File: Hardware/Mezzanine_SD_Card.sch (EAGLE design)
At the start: 9 parts, among them U1 USD-SOCKETNEW, U2 EDISON_CONNECTOR_FULLMOUNTING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, U3 EDISON_CONNECTOR_FULLHEADER

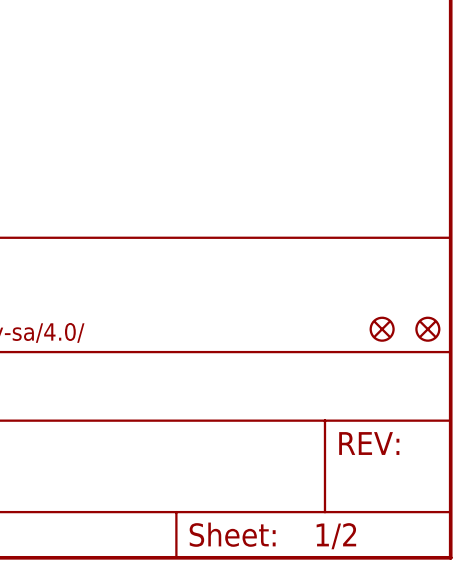
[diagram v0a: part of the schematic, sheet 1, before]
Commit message: added fiducials
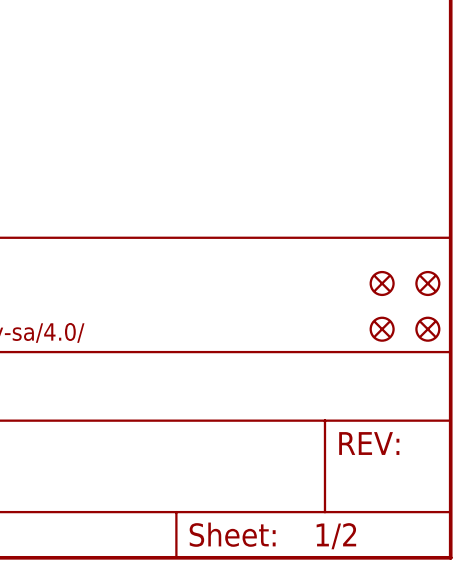
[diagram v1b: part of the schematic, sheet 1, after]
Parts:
- added FID3, FID4: FIDUCIAL1X2, SparkFun-Aesthetics:FIDUCIAL1X2
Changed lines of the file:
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@@
 <part name="U1" library="SparkFun-Connectors" deviceset="USD-SOCKET" device="NEW"/>
 <part name="GND1" library="SparkFun-Aesthetics" deviceset="GND" device=""/>
+<part name="FID3" library="SparkFun-Aesthetics" deviceset="FIDUCIAL" device="1X2"/>
+<part name="FID4" library="SparkFun-Aesthetics" deviceset="FIDUCIAL" device="1X2"/>
 </parts>
 <sheets>
@@
 <instance part="U1" gate="G$1" x="160.02" y="111.76"/>
 <instance part="GND1" gate="1" x="147.32" y="88.9"/>
+<instance part="FID3" gate="G$1" x="246.38" y="30.48"/>
+<instance part="FID4" gate="G$1" x="241.3" y="30.48"/>
 </instances>
 <busses>

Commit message: Layout complete, Ready for review.
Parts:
- added C1, C2: 0.1uF, SparkFun-Capacitors:0.1UF-25V(+80/-20%)(0603)
- added U$1: TXB0108, Testing:TXB0108
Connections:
- new net N$1: U$1.B1, U1.NC
- new net N$2: U$1.B2, U1.CS
- new net N$3: U$1.B3, U1.DI
- new net N$4: U$1.B4, U1.SCK
- new net N$5: U$1.B5, U1.DO
- new net N$6: U$1.B6, U1.RSV
- net 1.8V: now also C1.1, U$1.VCCA
- net 3.3V: now also C2.1, U$1.VCCB, U1.VCC
- net GND: now also C1.2, C2.2, U$1.GND, U$1.OE, U1.GND; no longer U1.SHIELD@2
- net GP77_SD_0_CD#: now also U1.SHIELD@2
- net GP78_SD_0_CLK: now also U$1.A4
- net GP79_SD_0_CMD: now also U$1.A3
- net GP80_SD_0_DAT0: now also U$1.A5
- net GP81_SD_0_DAT1: now also U$1.A6
- net GP82_SD_0_DAT2: now also U$1.A1
- net GP83_SD_0_DAT3: now also U$1.A2
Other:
- moved on the sheet: U1

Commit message: added version numbers
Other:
- note added: "Casey Kuhns"
- note added: "v01"
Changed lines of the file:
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@@
 <sheet>
 <plain>
+<text x="167.64" y="10.16" size="2.54" layer="94">Casey Kuhns</text>
+<text x="238.76" y="7.62" size="2.54" layer="94">v01</text>
 </plain>
 <instances>

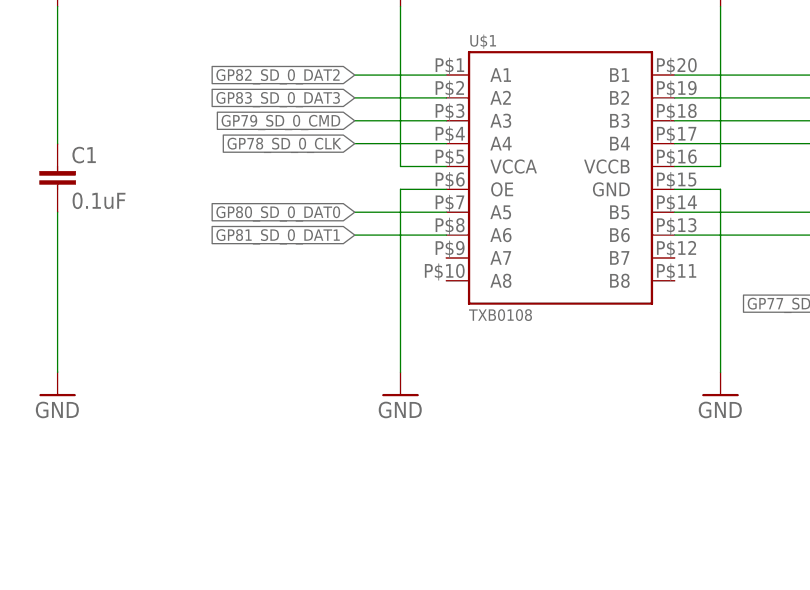
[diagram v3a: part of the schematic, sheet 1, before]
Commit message: fixed OE to high
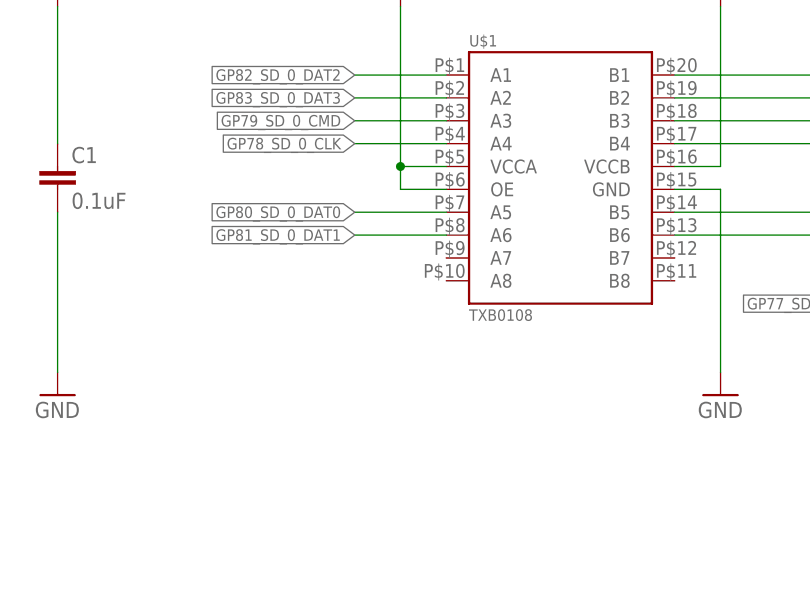
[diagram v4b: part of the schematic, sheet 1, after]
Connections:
- net 1.8V: now also U$1.OE
- net GND: no longer U$1.OE
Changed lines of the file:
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@@
 <part name="SUPPLY2" library="SparkFun-Aesthetics" deviceset="3.3V" device=""/>
 <part name="SUPPLY3" library="SparkFun-Aesthetics" deviceset="1.8V" device=""/>
-<part name="GND5" library="SparkFun-Aesthetics" deviceset="GND" device=""/>
 <part name="C1" library="SparkFun-Capacitors" deviceset="0.1UF-25V(+80/-20%)(0603)" device="" value="0.1uF"/>
 <part name="C2" library="SparkFun-Capacitors" deviceset="0.1UF-25V(+80/-20%)(0603)" device="" value="0.1uF"/>
@@
 <instance part="SUPPLY2" gate="G$1" x="160.02" y="132.08"/>
 <instance part="SUPPLY3" gate="G$1" x="104.14" y="132.08"/>
-<instance part="GND5" gate="1" x="104.14" y="88.9"/>
 <instance part="C1" gate="G$1" x="66.04" y="111.76"/>
 <instance part="C2" gate="G$1" x="198.12" y="109.22"/>
@@
 </segment>
 <segment>
-<pinref part="U$1" gate="G$1" pin="OE"/>
-<wire x1="109.22" y1="111.76" x2="104.14" y2="111.76" width="0.1524" layer="91"/>
-<wire x1="104.14" y1="111.76" x2="104.14" y2="91.44" width="0.1524" layer="91"/>
-<pinref part="GND5" gate="1" pin="GND"/>
-</segment>
-<segment>
 <pinref part="C1" gate="G$1" pin="2"/>
 <pinref part="GND6" gate="1" pin="GND"/>
@@
 <wire x1="109.22" y1="114.3" x2="104.14" y2="114.3" width="0.1524" layer="91"/>
 <wire x1="104.14" y1="114.3" x2="104.14" y2="132.08" width="0.1524" layer="91"/>
-</segment>
-<segment>
+<pinref part="U$1" gate="G$1" pin="OE"/>
+<wire x1="109.22" y1="111.76" x2="104.14" y2="111.76" width="0.1524" layer="91"/>
+<wire x1="104.14" y1="111.76" x2="104.14" y2="114.3" width="0.1524" layer="91"/>
+<junction x="104.14" y="114.3"/>
+</segment>
+<segment>

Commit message: work in progress
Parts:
- added SJ1, SJ2, SJ3: JUMPER-PAD-2-NO, SparkFun-Passives:JUMPER-PAD-2-NO
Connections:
- removed net N$4: U$1.B4, U1.SCK
- new net SCK: SJ3.2, U$1.B4, U$1.B7, U1.SCK
- new net SCK_FB: SJ1.2, U$1.A7
- net GP78_SD_0_CLK: now also SJ2.2
- net GP84_SD_CLK_FB: now also SJ1.1, SJ2.1, SJ3.1
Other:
- note added: "This is Casey Testing Clock FB Sources..."
- note added: "v02"
- note removed: "v01"
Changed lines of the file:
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@@
 <part name="GND7" library="SparkFun-Aesthetics" deviceset="GND" device=""/>
 <part name="SUPPLY5" library="SparkFun-Aesthetics" deviceset="3.3V" device=""/>
+<part name="SJ2" library="SparkFun-Passives" deviceset="JUMPER-PAD-2-NO" device=""/>
+<part name="SJ1" library="SparkFun-Passives" deviceset="JUMPER-PAD-2-NO" device=""/>
+<part name="SJ3" library="SparkFun-Passives" deviceset="JUMPER-PAD-2-NO" device=""/>
 </parts>
 <sheets>
@@
 <plain>
 <text x="167.64" y="10.16" size="2.54" layer="94">Casey Kuhns</text>
-<text x="238.76" y="7.62" size="2.54" layer="94">v01</text>
+<text x="238.76" y="7.62" size="2.54" layer="94">v02</text>
+<text x="93.98" y="76.2" size="1.778" layer="91">This is Casey Testing Clock FB Sources...</text>
 </plain>
 <instances>
@@
 <instance part="GND7" gate="1" x="198.12" y="88.9"/>
 <instance part="SUPPLY5" gate="G$1" x="198.12" y="132.08"/>
+<instance part="SJ2" gate="G$1" x="127" y="71.12"/>
+<instance part="SJ1" gate="G$1" x="127" y="63.5"/>
+<instance part="SJ3" gate="G$1" x="127" y="55.88"/>
 </instances>
 <busses>
@@
 <pinref part="U$1" gate="G$1" pin="A4"/>
 </segment>
+<segment>
+<pinref part="SJ2" gate="G$1" pin="2"/>
+<wire x1="132.08" y1="71.12" x2="134.62" y2="71.12" width="0.1524" layer="91"/>
+<label x="134.62" y="71.12" size="1.778" layer="95" xref="yes"/>
+</segment>
 </net>
 <net name="GP77_SD_0_CD#" class="0">
@@
 </segment>
 </net>
-<net name="N$4" class="0">
+<net name="SCK" class="0">
 <segment>
 <pinref part="U$1" gate="G$1" pin="B4"/>
-<wire x1="134.62" y1="116.84" x2="149.86" y2="116.84" width="0.1524" layer="91"/>
+<wire x1="134.62" y1="116.84" x2="142.24" y2="116.84" width="0.1524" layer="91"/>
+<wire x1="142.24" y1="116.84" x2="149.86" y2="116.84" width="0.1524" layer="91"/>
 <wire x1="149.86" y1="116.84" x2="149.86" y2="114.3" width="0.1524" layer="91"/>
 <pinref part="U1" gate="G$1" pin="SCK"/>
 <wire x1="149.86" y1="114.3" x2="165.1" y2="114.3" width="0.1524" layer="91"/>
+<pinref part="U$1" gate="G$1" pin="B7"/>
+<wire x1="134.62" y1="104.14" x2="142.24" y2="104.14" width="0.1524" layer="91"/>
+<wire x1="142.24" y1="104.14" x2="142.24" y2="116.84" width="0.1524" layer="91"/>
+<label x="144.78" y="116.84" size="1.778" layer="95"/>
+<junction x="142.24" y="116.84"/>
+</segment>
+<segment>
+<pinref part="SJ3" gate="G$1" pin="2"/>
+<wire x1="132.08" y1="55.88" x2="134.62" y2="55.88" width="0.1524" layer="91"/>
+<label x="134.62" y="55.88" size="1.778" layer="95" xref="yes"/>
 </segment>
 </net>
@@
 </segment>
 </net>
+<net name="GP84_SD_CLK_FB" class="0">
+<segment>
+<pinref part="SJ2" gate="G$1" pin="1"/>
+<wire x1="121.92" y1="71.12" x2="119.38" y2="71.12" width="0.1524" layer="91"/>
+<wire x1="119.38" y1="71.12" x2="119.38" y2="63.5" width="0.1524" layer="91"/>
+<pinref part="SJ1" gate="G$1" pin="1"/>
+<wire x1="119.38" y1="63.5" x2="121.92" y2="63.5" width="0.1524" layer="91"/>
+<wire x1="119.38" y1="63.5" x2="119.38" y2="60.96" width="0.1524" layer="91"/>
+<pinref part="SJ3" gate="G$1" pin="1"/>
+<wire x1="119.38" y1="60.96" x2="119.38" y2="55.88" width="0.1524" layer="91"/>
+<wire x1="119.38" y1="55.88" x2="121.92" y2="55.88" width="0.1524" layer="91"/>
+<wire x1="119.38" y1="60.96" x2="114.3" y2="60.96" width="0.1524" layer="91"/>
+<junction x="119.38" y="60.96"/>
+<label x="114.3" y="60.96" size="1.778" layer="95" rot="R180" xref="yes"/>
+</segment>
+</net>
+<net name="SCK_FB" class="0">
+<segment>
+<pinref part="U$1" gate="G$1" pin="A7"/>
+<wire x1="109.22" y1="104.14" x2="104.14" y2="104.14" width="0.1524" layer="91"/>
+<label x="104.14" y="104.14" size="1.778" layer="95" rot="R180" xref="yes"/>
+</segment>
+<segment>
+<pinref part="SJ1" gate="G$1" pin="2"/>
+<wire x1="132.08" y1="63.5" x2="134.62" y2="63.5" width="0.1524" layer="91"/>
+<label x="134.62" y="63.5" size="1.778" layer="95" xref="yes"/>
+</segment>
+</net>

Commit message: work in progress
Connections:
- new net DCIN: U2.DCIN, U3.DCIN
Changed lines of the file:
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@@
+</segment>
+</net>
+<net name="DCIN" class="0">
+<segment>
+<pinref part="U2" gate="G$1" pin="DCIN"/>
+<wire x1="25.4" y1="152.4" x2="22.86" y2="152.4" width="0.1524" layer="91"/>
+<label x="22.86" y="152.4" size="1.27" layer="95" rot="R180" xref="yes"/>
+</segment>
+<segment>
+<pinref part="U3" gate="G$1" pin="DCIN"/>
+<wire x1="172.72" y1="152.4" x2="170.18" y2="152.4" width="0.1524" layer="91"/>
+<label x="170.18" y="152.4" size="1.27" layer="95" rot="R180" xref="yes"/>
 </segment>
 </net>

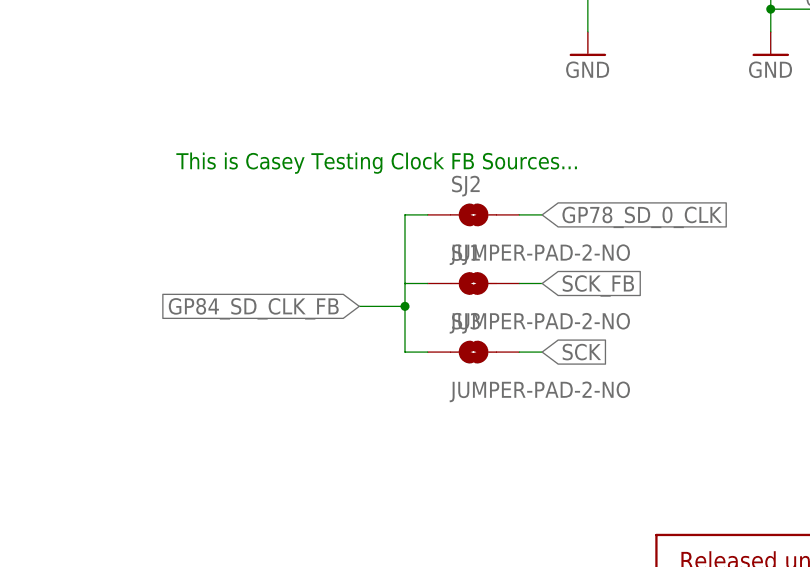
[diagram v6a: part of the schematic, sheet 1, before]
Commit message: Added DCIN pin cleaned up dimensions cleaned up names on board created clock feedback test circuit
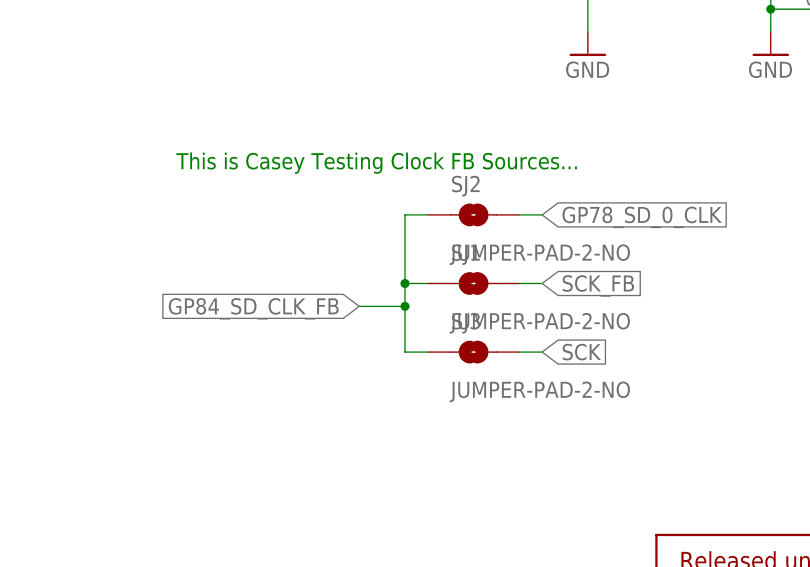
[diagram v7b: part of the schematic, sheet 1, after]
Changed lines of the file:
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@@
 <junction x="119.38" y="60.96"/>
 <label x="114.3" y="60.96" size="1.778" layer="95" rot="R180" xref="yes"/>
+<junction x="119.38" y="63.5"/>
 </segment>
 </net>
